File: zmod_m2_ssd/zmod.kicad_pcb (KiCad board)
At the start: 6 copper layers, 50 x 70 mm, 23 parts, among them J1 MDT420M02001, J2 QTH-020-01-X-D-DP-A, U1 SN74LVC1T45DBV, U2 LTC6957xMS-2, X1 ECS-2520MVQ-1000-BN-TR

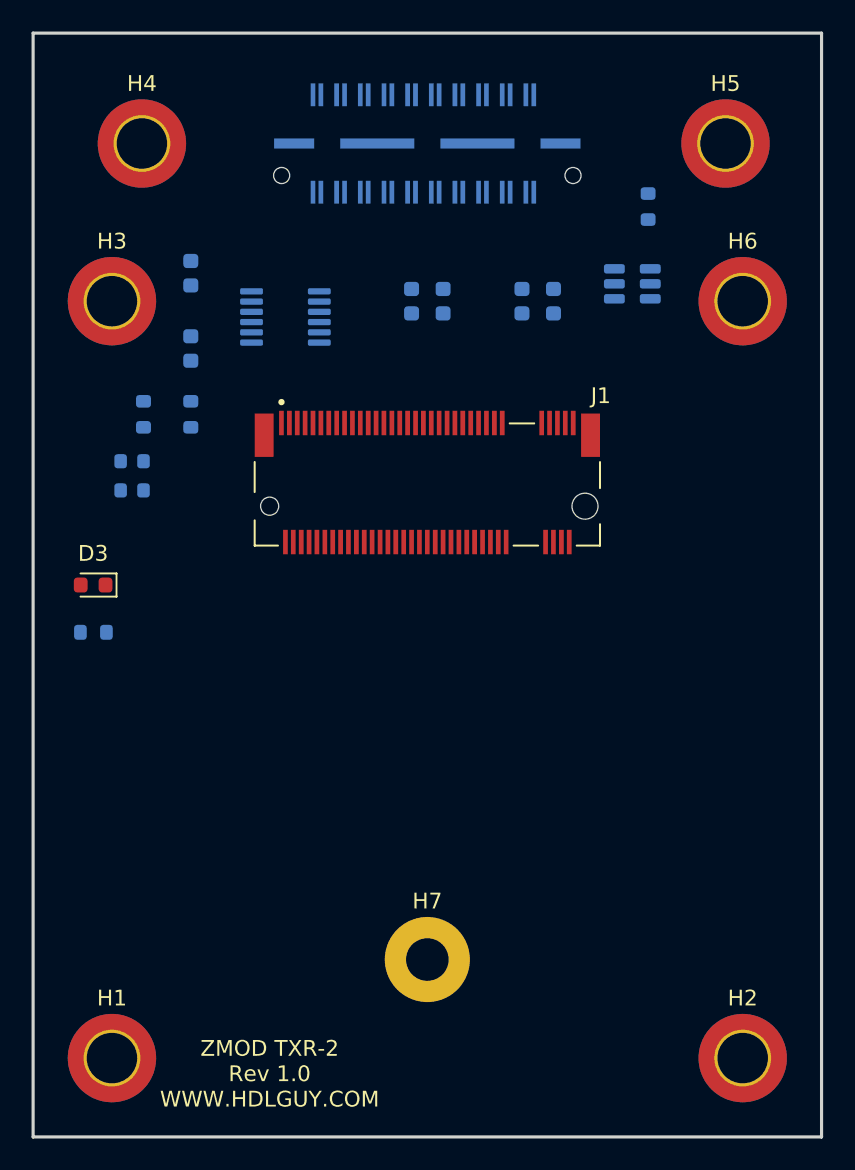
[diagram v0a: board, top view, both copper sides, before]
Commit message: first cut at routing the m.2 zmod
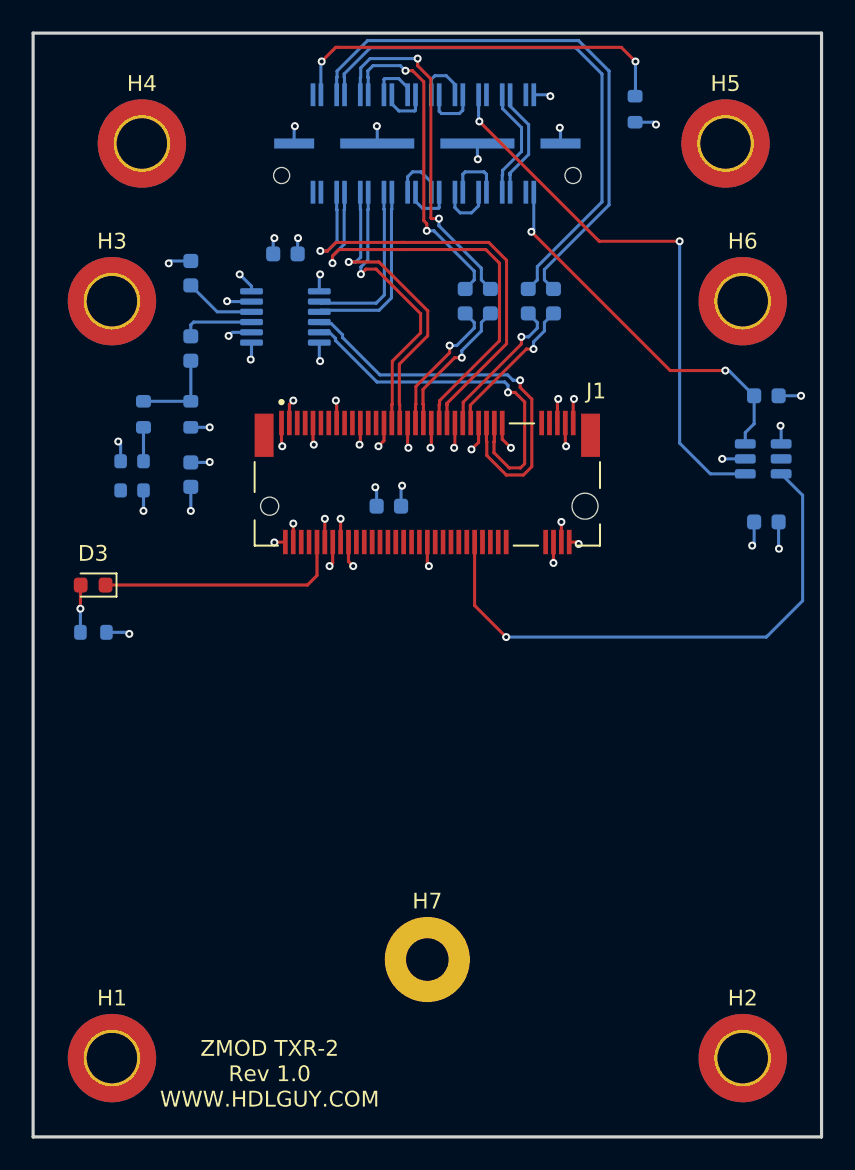
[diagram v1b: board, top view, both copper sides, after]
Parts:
- added C10: 0.01uf, Capacitor_SMD:C_0603_1608Metric, B.Cu at (146.5, 73.0)
- added C11: 0.01uf, Capacitor_SMD:C_0603_1608Metric, B.Cu at (116.0, 64.0)
- added C7: 0.01uf, Capacitor_SMD:C_0603_1608Metric, B.Cu at (110.0, 78.0)
- added C8: 0.01uf, Capacitor_SMD:C_0603_1608Metric, B.Cu at (122.6, 80.0)
- added C9: 0.01uf, Capacitor_SMD:C_0603_1608Metric, B.Cu at (146.5, 81.0)
- moved U1 13.9 mm to (146.3, 77.0)
- moved R5 6.23 mm to (138.2, 54.8)
- moved C2 3.40 mm to (127.4, 67.0)
- moved C4 3.00 mm to (129.0, 67.0)
- moved C1 0.40 mm to (131.4, 67.0)
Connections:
- net /gtr0_rxn renamed /gtr0_rx_N
- net /gtr0_rxp renamed /gtr0_rx_P
- net /gtr0_txn renamed /gtr0_tx_N
- net /gtr0_txn_cc renamed /gtr0_tx_cc_N
- net /gtr0_txp renamed /gtr0_tx_P
- net /gtr0_txp_cc renamed /gtr0_tx_cc_P
- net /gtr1_rxn renamed /gtr1_rx_N
- net /gtr1_rxp renamed /gtr1_rx_P
- net /gtr1_txn renamed /gtr1_tx_N
- net /gtr1_txn_cc renamed /gtr1_tx_cc_N
- net /gtr1_txp renamed /gtr1_tx_P
- net /gtr1_txp_cc renamed /gtr1_tx_cc_P
- net /gtrclk0_n renamed /gtrclk0_N
- net /gtrclk0_p renamed /gtrclk0_P
- net Net-(J1-Pad50) renamed /perst_n
- net Net-(J2-Pad30) renamed /perst_1v8
- J1 pad 53: Net-(J1-Pad53) -> /pcie_refclk_N
- J1 pad 55: Net-(J1-Pad55) -> /pcie_refclk_P
- U2 pad 10: Net-(J1-Pad55) -> /pcie_refclk_N
- U2 pad 11: Net-(J1-Pad53) -> /pcie_refclk_P
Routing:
- net GND: track 0.00 -> 44.7 mm, vias 0 -> 32
- net /gtr0_tx_P: track 0.00 -> 36.1 mm
- net /perst_1v8: track 0.00 -> 35.3 mm, vias 0 -> 2
- net /perst_n: track 0.00 -> 35.2 mm, vias 0 -> 1
- net /gtr0_tx_N: track 0.00 -> 34.6 mm
- net /gtr0_rx_P: track 0.00 -> 29.1 mm, vias 0 -> 1
- net /gtr0_rx_N: track 0.00 -> 28.2 mm, vias 0 -> 1
- net +3V3: track 0.00 -> 26.2 mm, vias 0 -> 20
- net /pcie_refclk_N: track 0.00 -> 25.8 mm, vias 0 -> 1
- net /R_GA: track 0.00 -> 25.0 mm, vias 0 -> 2
- net +1V8: track 0.00 -> 24.3 mm, vias 0 -> 2
- net /pcie_refclk_P: track 0.00 -> 23.6 mm, vias 0 -> 1
- net /gtr1_tx_P: track 0.00 -> 22.4 mm, vias 0 -> 2
- net /gtr1_tx_N: track 0.00 -> 20.6 mm, vias 0 -> 2
- net /gtr1_rx_P: track 0.00 -> 19.2 mm, vias 0 -> 1
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- added copper zone on In1.Cu, net +3V3
- added copper zone on In2.Cu, net GND
- removed copper zone on In3.Cu, net +3V3
- removed copper zone on In4.Cu, net GND
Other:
- copper layers 6 -> 4

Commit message: ready to send to Oshpark
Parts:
- removed R5: 10k,1%, Resistor_SMD:R_0603_1608Metric
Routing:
- net /R_GA: track 25.0 -> 0.00 mm, vias 2 -> 0
- net /gtr0_rx_N: track 28.2 -> 22.0 mm
- net /gtr0_rx_P: track 29.1 -> 23.1 mm
- net +3V3: track 26.2 -> 24.4 mm, vias 20 -> 19
- net /gtrclk0_P: track 10.9 -> 9.54 mm
- net /gtrclk0_N: track 11.7 -> 10.3 mm
- net /gtr1_rx_P: track 19.2 -> 17.9 mm
- net GND: track 44.7 -> 46.0 mm, vias 32 -> 33
- net /gtr1_rx_N: track 18.2 -> 16.9 mm
- net /gtr0_tx_cc_P: track 9.41 -> 10.2 mm
- net /gtr0_tx_cc_N: track 9.41 -> 9.97 mm
- removed copper zone on In2.Cu, net +3V3
- removed copper zone on In1.Cu, net GND

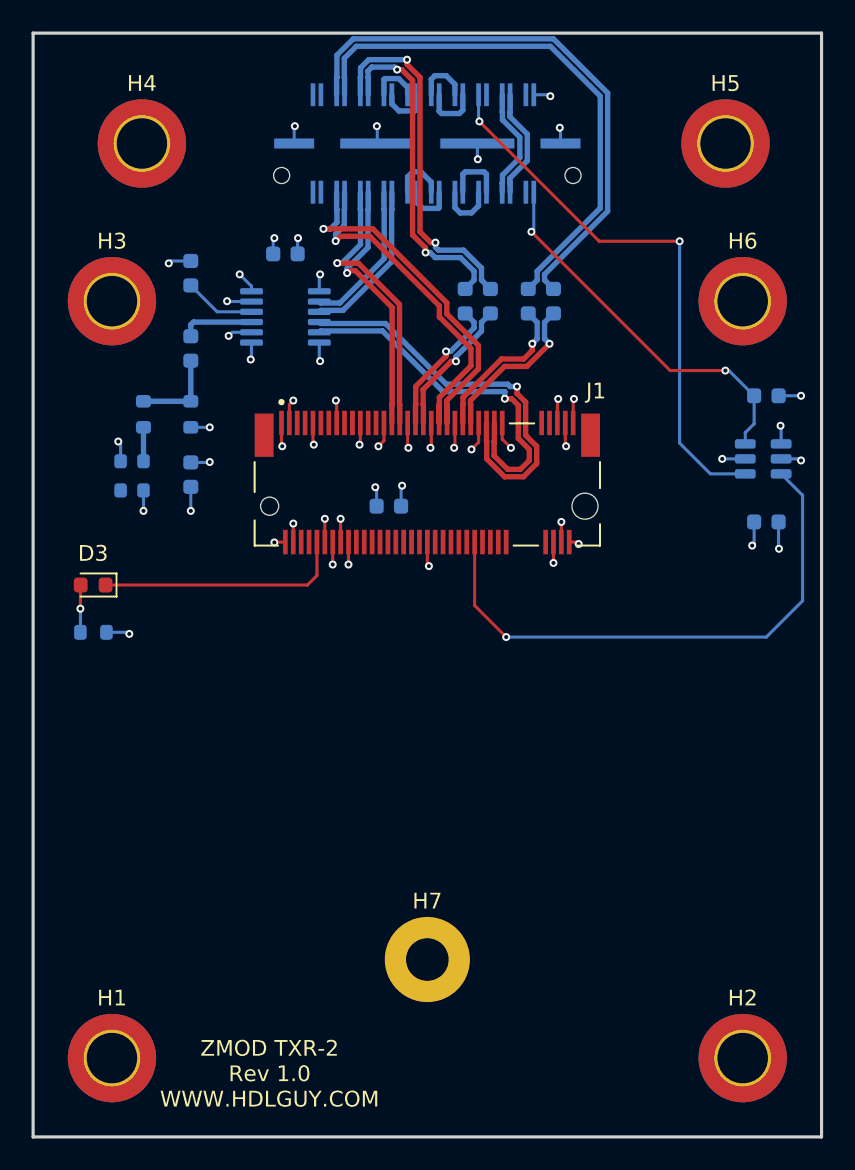
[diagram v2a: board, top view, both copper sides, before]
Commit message: updated oscilltor symbol and footprint to have 3D model
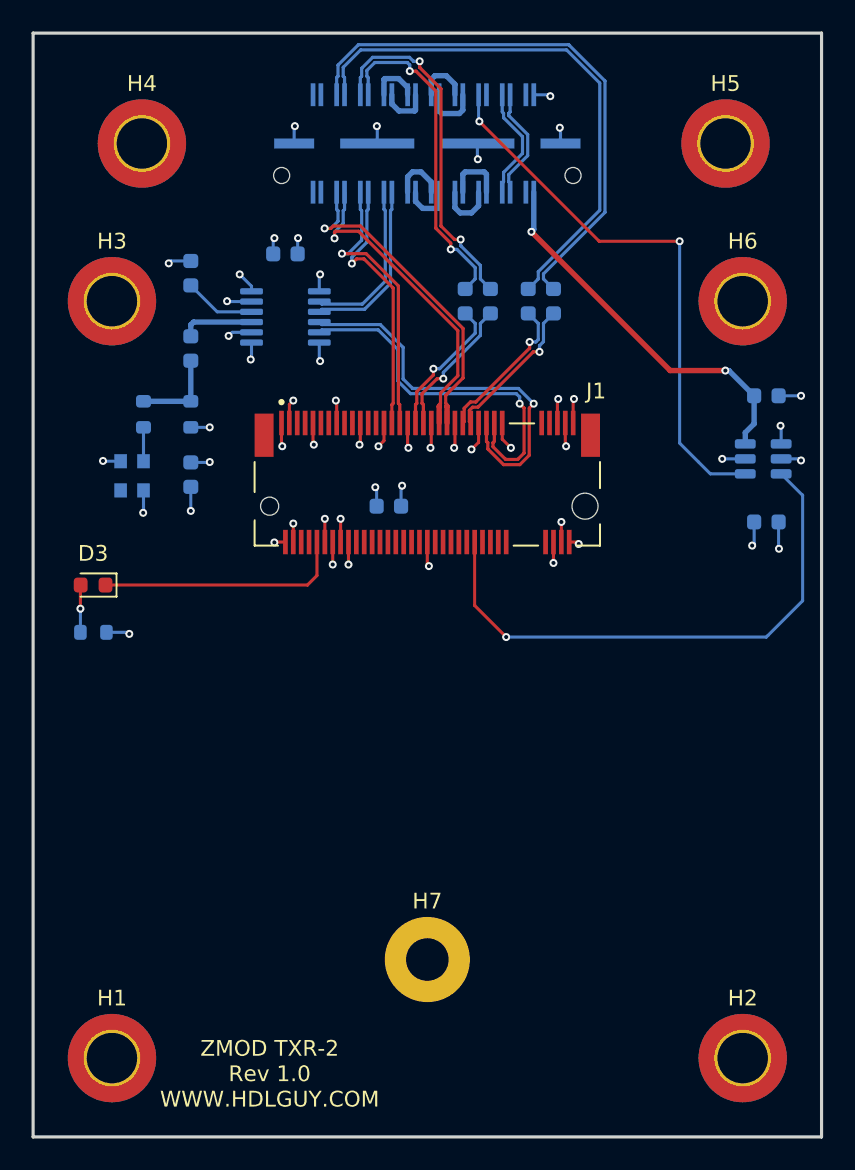
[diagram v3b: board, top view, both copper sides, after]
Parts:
- X1: footprint Oscillator:Oscillator_SMD_ECS_2520MV-xxx-xx-4Pin_2.5x2.0mm -> pedrolib:OSC_ECS-2520S25-250-FN-TR
- turned X1 to 90 degrees
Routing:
- net /gtr0_rx_P: track 23.1 -> 22.0 mm
- net /gtrclk0_P: track 9.54 -> 10.5 mm
- net /gtrclk0_N: track 10.3 -> 11.1 mm
- net /pcie_refclk_N: track 25.9 -> 25.3 mm
- net /gtr0_tx_cc_P: track 10.2 -> 9.63 mm
- net /gtr0_rx_N: track 22.0 -> 21.5 mm

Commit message: Rev B of zmod M.2, changed clock buffer to give full edge rate, reduced M.2 mounting hole from 2.7 to 2.5 mm
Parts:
- H7: footprint MountingHole:MountingHole_2.7mm_Pad -> MountingHole:MountingHole_2.5mm_Pad
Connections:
- U2 pad 6: +3V3 -> GND
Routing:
- net GND: track 45.8 -> 47.2 mm, vias 33 -> 34
- net +3V3: track 24.5 -> 23.2 mm, vias 19 -> 18
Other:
- board text added: "ZMOD TXR-2, Rev B Rev 1.0 WWW.HDLGUY.COM"
- board text removed: "ZMOD TXR-2 Rev 1.0 WWW.HDLGUY.COM"
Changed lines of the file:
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@@
   (net 82 "/pcie_refclk_P")
   (net 83 "/pcie_refclk_N")
-  (footprint "MountingHole:MountingHole_2.7mm_Pad" locked (layer "F.Cu")
+  (footprint "MountingHole:MountingHole_2.5mm_Pad" locked (layer "F.Cu")
     (at 125 108.75)
-    (descr "Mounting Hole 2.7mm")
-    (tags "mounting hole 2.7mm")
+    (descr "Mounting Hole 2.5mm")
+    (tags "mounting hole 2.5mm")
     (property "Sheetfile" "zmod.kicad_sch")
     (property "Sheetname" "")
     (attr exclude_from_pos_files)
-    (fp_text reference "H7" (at 0 -3.7) (layer "F.SilkS")
-      (effects (font (size 1 1) (thickness 0.15)))
-    )
-    (fp_text value "MountingHole_Pad" (at 0 3.7) (layer "F.Fab")
+    (fp_text reference "H7" (at 0 -3.5) (layer "F.SilkS")
+      (effects (font (size 1 1) (thickness 0.15)))
+    )
+    (fp_text value "MountingHole_Pad" (at 0 3.5) (layer "F.Fab") hide
       (effects (font (size 1 1) (thickness 0.15)))
     )
@@
       (effects (font (size 1 1) (thickness 0.15)))
     )
-    (fp_circle (center 0 0) (end 2.7 0) (layer "Cmts.User") (width 0.15) (fill none))
-    (fp_circle (center 0 0) (end 2.95 0) (layer "F.CrtYd") (width 0.05) (fill none))
-    (pad "1" thru_hole circle locked (at 0 0) (size 5.4 5.4) (drill 2.7) (layers *.Cu *.Mask)
+    (fp_circle (center 0 0) (end 2.5 0) (layer "Cmts.User") (width 0.15) (fill none))
+    (fp_circle (center 0 0) (end 2.75 0) (layer "F.CrtYd") (width 0.05) (fill none))
+    (pad "1" thru_hole circle locked (at 0 0) (size 5 5) (drill 2.5) (layers *.Cu *.Mask)
       (net 54 "unconnected-(H7-Pad1)") (pinfunction "1") (pintype "input"))
   )
@@
       (net 1 "GND") (pinfunction "GND") (pintype "power_in"))
     (pad "6" smd roundrect (at -2.15 -1.625) (size 1.45 0.4) (layers "B.Cu" "B.Paste" "B.Mask") (roundrect_rratio 0.25)
-      (net 6 "+3V3") (pinfunction "FILTB") (pintype "input"))
+      (net 1 "GND") (pinfunction "FILTB") (pintype "input"))
     (pad "7" smd roundrect (at 2.15 -1.625) (size 1.45 0.4) (layers "B.Cu" "B.Paste" "B.Mask") (roundrect_rratio 0.25)
       (net 1 "GND") (pinfunction "SD2") (pintype "input"))
@@
   (gr_line locked (start 100 120) (end 150 120) (layer "Edge.Cuts") (width 0.2))
   (gr_line locked (start 150 120) (end 150 50) (layer "Edge.Cuts") (width 0.2))
-  (gr_text "ZMOD TXR-2\nRev 1.0\nWWW.HDLGUY.COM" (at 115 116) (layer "F.SilkS")
+  (gr_text "ZMOD TXR-2, Rev B\nRev 1.0\nWWW.HDLGUY.COM" (at 125.222 115.1636) (layer "F.SilkS")
     (effects (font (size 1 1) (thickness 0.15)))
   )
@@
   (via (at 116.5 73.3) (size 0.508) (drill 0.254) (layers "F.Cu" "B.Cu") (net 1))
   (via (at 145.6 82.5) (size 0.508) (drill 0.254) (layers "F.Cu" "B.Cu") (net 1))
+  (via (at 113.1 65.3) (size 0.508) (drill 0.254) (layers "F.Cu" "B.Cu") (net 1))
   (via (at 133.8 76.2) (size 0.508) (drill 0.254) (layers "F.Cu" "B.Cu") (net 1))
   (via (at 111.2 75) (size 0.508) (drill 0.254) (layers "F.Cu" "B.Cu") (net 1))
@@
   (segment (start 118.15 65.35) (end 118.2 65.3) (width 0.19558) (layer "B.Cu") (net 1))
   (segment (start 145.1625 77) (end 143.7 77) (width 0.19558) (layer "B.Cu") (net 1))
+  (segment (start 113.85 66.05) (end 113.1 65.3) (width 0.19558) (layer "B.Cu") (net 1))
   (segment (start 113.85 67.025) (end 112.325 67.025) (width 0.19558) (layer "B.Cu") (net 1))
   (segment (start 145.725 82.375) (end 145.6 82.5) (width 0.19558) (layer "B.Cu") (net 1))
@@
   (segment (start 118.15 66.375) (end 118.15 65.35) (width 0.19558) (layer "B.Cu") (net 1))
   (segment (start 118.15 69.625) (end 118.15 70.75) (width 0.19558) (layer "B.Cu") (net 1))
+  (segment (start 113.85 66.375) (end 113.85 66.05) (width 0.19558) (layer "B.Cu") (net 1))
   (segment (start 116.555 57) (end 116.555 55.945) (width 0.19558) (layer "B.Cu") (net 1))
   (segment (start 119 82.275) (end 119 83.7) (width 0.19558) (layer "F.Cu") (net 6))
@@
   (via (at 147.4 74.9) (size 0.508) (drill 0.254) (layers "F.Cu" "B.Cu") (net 6))
   (via (at 134.6 82.4) (size 0.508) (drill 0.254) (layers "F.Cu" "B.Cu") (net 6))
-  (via (at 113.1 65.3) (size 0.508) (drill 0.254) (layers "F.Cu" "B.Cu") (net 6))
   (via (at 112.4 69.2) (size 0.508) (drill 0.254) (layers "F.Cu" "B.Cu") (net 6))
   (via (at 119.5 80.8) (size 0.508) (drill 0.254) (layers "F.Cu" "B.Cu") (net 6))
@@
   (segment (start 110 78.775) (end 110 80.3) (width 0.19558) (layer "B.Cu") (net 6))
   (segment (start 104.65 88) (end 106 88) (width 0.19558) (layer "B.Cu") (net 6))
-  (segment (start 113.85 66.05) (end 113.1 65.3) (width 0.19558) (layer "B.Cu") (net 6))
   (segment (start 147.4375 76.05) (end 147.4375 74.9375) (width 0.19558) (layer "B.Cu") (net 6))
   (segment (start 131.75 53.91) (end 132.71 53.91) (width 0.19558) (layer "B.Cu") (net 6))
@@
   (segment (start 113.85 68.975) (end 112.625 68.975) (width 0.19558) (layer "B.Cu") (net 6))
   (segment (start 121.785 80) (end 121.785 78.885) (width 0.19558) (layer "B.Cu") (net 6))
-  (segment (start 113.85 66.375) (end 113.85 66.05) (width 0.19558) (layer "B.Cu") (net 6))
   (segment (start 104.5925 85) (end 117.4 85) (width 0.19558) (layer "F.Cu") (net 30))
   (segment (start 118 84.4) (end 118 82.275) (width 0.19558) (layer "F.Cu") (net 30))
@@
   (segment (start 110 66) (end 111.675 67.675) (width 0.19558) (layer "B.Cu") (net 42))
   (segment (start 111.675 67.675) (end 113.85 67.675) (width 0.19558) (layer "B.Cu") (net 42))
-  (segment (start 107 73.35) (end 110 73.35) (width 0.3429) (layer "B.Cu") (net 43))
-  (segment (start 110 73.35) (end 110 70.775) (width 0.3429) (layer "B.Cu") (net 43))
+  (segment (start 107 73.35) (end 110 73.35) (width 0.2032) (layer "B.Cu") (net 43))
+  (segment (start 110 73.35) (end 110 70.775) (width 0.2032) (layer "B.Cu") (net 43))
   (segment (start 131.6 62.6) (end 140.4 71.4) (width 0.3429) (layer "F.Cu") (net 52))
   (segment (start 140.4 71.4) (end 143.9 71.4) (width 0.3429) (layer "F.Cu") (net 52))
@@
   (segment (start 131.75 62.45) (end 131.6 62.6) (width 0.3429) (layer "B.Cu") (net 52))
   (segment (start 144.125 71.4) (end 145.725 73) (width 0.3429) (layer "B.Cu") (net 52))
-  (segment (start 110 69.225) (end 110 68.5) (width 0.3429) (layer "B.Cu") (net 53))
-  (segment (start 110.175 68.325) (end 113.85 68.325) (width 0.3429) (layer "B.Cu") (net 53))
-  (segment (start 110 68.5) (end 110.175 68.325) (width 0.3429) (layer "B.Cu") (net 53))
+  (segment (start 110 69.225) (end 110 68.5) (width 0.2032) (layer "B.Cu") (net 53))
+  (segment (start 110.175 68.325) (end 113.85 68.325) (width 0.2032) (layer "B.Cu") (net 53))
+  (segment (start 110 68.5) (end 110.175 68.325) (width 0.2032) (layer "B.Cu") (net 53))
   (segment (start 107 77.15) (end 107 75) (width 0.19558) (layer "B.Cu") (net 55))
   (segment (start 135.9 63.2) (end 128.3 55.6) (width 0.19558) (layer "F.Cu") (net 57))
